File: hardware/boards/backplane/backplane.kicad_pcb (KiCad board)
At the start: 4 copper layers, 151.8 x 30.8 mm, 90 parts, among them J1 XT30U_2+2, J10 SWD, J11 12V 3-WIRE FAN, J12 DS18B20 EXT SUPPLY, J2 XT30U_2+2, J3 XT30U_2+2, J4 XT30U_2+2, J5 XT30U_2+2, J6 XT30U_2+2, J7 XY308-2.54-3P / EXTERNAL CAN, J8 DC IN, J9 12V 3-WIRE FAN, Q1 AO3407A, Q2 2N7002, Q3 AO3407A, Q4 2N7002, U1 STM32C092GCU6, U2 LM5164DDAR, U3 LM5164DDAR, U4 INA237AIDGSR, U5 TCAN3413DR

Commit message: Checkpoint review artifacts and prototype layout refinements
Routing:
- net GND: track 57.7 -> 57.1 mm, vias 66 -> 70
- net VIN_RAW: track 5.21 -> 5.75 mm
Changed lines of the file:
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@@
 	)
 	(segment
-		(start 108.609552 72.588273)
-		(end 108.609552 73.254047)
-		(width 0.2)
-		(layer "F.Cu")
-		(net "GND")
-	)
-	(segment
 		(start 74.603519 50.287638)
 		(end 74.299136 50.592021)
@@
 	)
 	(via
+		(at 109.212052 72.015233)
+		(size 0.6)
+		(drill 0.3)
+		(layers "F.Cu" "B.Cu")
+		(net "GND")
+	)
+	(via
 		(at 109.5425 57.420624)
 		(size 0.6)
@@
 	)
 	(via
-		(at 164.699054 68.604999)
+		(at 131.53 76.517182)
 		(size 0.6)
 		(drill 0.3)
@@
 	)
 	(via
-		(at 131.53 76.517182)
+		(at 137.77 76.517182)
 		(size 0.6)
 		(drill 0.3)
@@
 	)
 	(via
-		(at 137.77 76.517182)
+		(at 113.283564 76.7)
 		(size 0.6)
 		(drill 0.3)
 		(layers "F.Cu" "B.Cu")
-		(free yes)
 		(net "GND")
 	)
@@
 	)
 	(via
+		(at 114.999552 74.787302)
+		(size 0.6)
+		(drill 0.3)
+		(layers "F.Cu" "B.Cu")
+		(net "GND")
+	)
+	(via
 		(at 173.16272 72.052896)
 		(size 0.6)
@@
 	)
 	(via
+		(at 164.137319 67.764828)
+		(size 0.6)
+		(drill 0.3)
+		(layers "F.Cu" "B.Cu")
+		(free yes)
+		(net "GND")
+	)
+	(via
 		(at 75.774011 53.09876)
 		(size 0.6)
@@
 	)
 	(via
+		(at 118.259552 74.787302)
+		(size 0.6)
+		(drill 0.3)
+		(layers "F.Cu" "B.Cu")
+		(net "GND")
+	)
+	(via
 		(at 173.16272 74.352544)
 		(size 0.6)
@@
 	)
 	(via
-		(at 161.836855 68.604999)
+		(at 161.836855 65.295)
 		(size 0.6)
 		(drill 0.3)
@@
 	)
 	(via
-		(at 161.836855 65.295)
+		(at 75.774011 57.420624)
 		(size 0.6)
 		(drill 0.3)
@@
 	)
 	(via
-		(at 75.774011 57.420624)
+		(at 162.411231 67.78024)
 		(size 0.6)
 		(drill 0.3)
@@
 	)
 	(segment
-		(start 165.5975 69.38569)
-		(end 165.5975 67.5625)
+		(start 166.717857 71.254645)
+		(end 167.039487 71.254645)
 		(width 0.2)
 		(layer "F.Cu")
@@
 	)
 	(segment
-		(start 167.039487 70.827677)
-		(end 167.039487 71.304645)
+		(start 165.108243 69.645031)
+		(end 166.717857 71.254645)
 		(width 0.2)
 		(layer "F.Cu")
@@
 	)
 	(segment
-		(start 165.5975 69.38569)
-		(end 167.039487 70.827677)
+		(start 165.108243 68.051757)
+		(end 165.108243 69.645031)
 		(width 0.2)
 		(layer "F.Cu")
@@
 	)
 	(segment
-		(start 165.5975 67.5625)
-		(end 166.21 66.95)
+		(start 166.21 66.95)
+		(end 165.108243 68.051757)
 		(width 0.2)
 		(layer "F.Cu")
@@
 	)
 	(segment
-		(start 160.8975 69.007922)
-		(end 159.271816 70.633606)
+		(start 161.539437 68.204437)
+		(end 161.539437 69.750946)
 		(width 0.2)
 		(layer "F.Cu")
@@
 	)
 	(segment
-		(start 159.728882 71.304645)
-		(end 159.271816 71.304645)
+		(start 162.277468 73.853231)
+		(end 159.728882 71.304645)
 		(width 0.2)
 		(layer "F.Cu")
@@
 	)
 	(segment
-		(start 162.277468 73.853231)
-		(end 159.728882 71.304645)
-		(width 0.2)
-		(layer "F.Cu")
-		(net "VCC")
-	)
-	(segment
-		(start 160.8975 69.007922)
-		(end 160.8975 67.5625)
+		(start 161.539437 69.750946)
+		(end 160.953316 70.337067)
 		(width 0.2)
 		(layer "F.Cu")
@@
 	)
 	(segment
-		(start 160.8975 67.5625)
-		(end 160.285 66.95)
-		(width 0.2)
-		(layer "F.Cu")
-		(net "VCC")
-	)
-	(segment
 		(start 150.3225 74.72)
 		(end 151.565 74.72)
@@
 	)
 	(segment
+		(start 160.285 66.95)
+		(end 161.539437 68.204437)
+		(width 0.2)
+		(layer "F.Cu")
+		(net "VCC")
+	)
+	(segment
 		(start 151.565 74.72)
 		(end 153.33 72.955)
@@
 	)
 	(segment
-		(start 159.271816 70.633606)
-		(end 159.271816 71.304645)
+		(start 160.953316 70.337067)
+		(end 160.189394 70.337067)
 		(width 0.2)
 		(layer "F.Cu")
@@
 		(net "VCC")
 	)
+	(segment
+		(start 160.189394 70.337067)
+		(end 159.271816 71.254645)
+		(width 0.2)
+		(layer "F.Cu")
+		(net "VCC")
+	)
 	(via
 		(at 154.15 68.75)
@@
 		(net "VCC")
 		(layer "F.Cu")
-		(name "VIN_BUS_BACK")
+		(name "VIN_BUS_FRONT")
 		(hatch edge 0.5)
 		(priority 1)
@@
 		(polygon
 			(pts
-				(xy 161.82 63.94) (xy 42.55 63.94) (xy 42.55 71.938594) (xy 89.003284 71.938594) (xy 89.003284 69.45)
-				(xy 158.483546 69.45) (xy 158.483546 70.298636) (xy 161.82 70.298636)
+				(xy 161.100644 63.94) (xy 42.55 63.94) (xy 42.55 71.938594) (xy 89.003284 71.938594) (xy 89.003284 69.45)
+				(xy 158.483546 69.45) (xy 158.483546 69.897828) (xy 161.100644 69.897828)
 			)
 		)
@@
 		(polygon
 			(pts
-				(xy 178.801504 62.512966) (xy 164.55 62.512966) (xy 164.55 70.401526) (xy 167.85331 70.401526) (xy 167.85331 70.4)
-				(xy 178.801504 70.4)
+				(xy 178.801504 62.512966) (xy 165.270064 62.512966) (xy 165.516648 69.367624) (xy 166.665067 69.588822)
+				(xy 166.664665 70.400937) (xy 167.85331 70.401526) (xy 167.85331 70.4) (xy 178.801504 70.4)
 			)
 		)
@@
 		(net "VCC")
 		(layer "B.Cu")
-		(name "VCC_FRONT")
+		(name "VCC_BACK")
 		(hatch edge 0.5)
 		(priority 3)
@@
 		(net "VCC")
 		(layer "In1.Cu")
-		(name "VCC_IN2")
+		(name "VCC_IN1")
 		(hatch edge 0.5)
 		(priority 3)
@@
 		(net "VCC")
 		(layer "In2.Cu")
-		(name "VCC_IN1")
+		(name "VCC_IN2_1")
 		(hatch edge 0.5)
 		(priority 3)

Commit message: Refine prototype Kelvin pours and input grounding; add test TODOs
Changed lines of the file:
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@@
 					(thickness 0.15)
 				)
+				(justify mirror)
 			)
 		)
@@
 			(pinfunction "Pin_1_1")
 			(pintype "passive")
+			(zone_connect 2)
 		)
 		(pad "2" thru_hole circle
@@
 			(pinfunction "Pin_2_2")
 			(pintype "passive")
+			(zone_connect 2)
 		)
 		(embedded_fonts no)
@@
 	(segment
 		(start 162.277468 73.853231)
-		(end 159.728882 71.304645)
+		(end 159.678882 71.254645)
 		(width 0.2)
 		(layer "F.Cu")
@@
 	)
 	(segment
+		(start 159.678882 71.254645)
+		(end 159.271816 71.254645)
+		(width 0.2)
+		(layer "F.Cu")
+		(net "VCC")
+	)
+	(segment
 		(start 160.189394 70.337067)
 		(end 159.271816 71.254645)
@@
 		(polygon
 			(pts
-				(xy 161.100644 63.94) (xy 42.55 63.94) (xy 42.55 71.938594) (xy 89.003284 71.938594) (xy 89.003284 69.45)
-				(xy 158.483546 69.45) (xy 158.483546 69.897828) (xy 161.100644 69.897828)
+				(xy 160.8975 63.94) (xy 42.55 63.94) (xy 42.55 71.94) (xy 89 71.94) (xy 89 69.45) (xy 158.48 69.45)
+				(xy 158.48 69.9) (xy 160.8975 69.9)
 			)
 		)
@@
 		(polygon
 			(pts
-				(xy 178.801504 62.512966) (xy 165.270064 62.512966) (xy 165.516648 69.367624) (xy 166.665067 69.588822)
-				(xy 166.664665 70.400937) (xy 167.85331 70.401526) (xy 167.85331 70.4) (xy 178.801504 70.4)
+				(xy 178.8 62.51) (xy 165.5975 62.51) (xy 165.5975 68.625) (xy 166.95 68.625) (xy 166.95 70.4) (xy 178.8 70.4)
 			)
 		)

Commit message: Add PCBWay logo footprint and stage artwork above both boards
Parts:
- added LOGO_PCBWAY: PCBWay_Logo_25mm, mini-rack-power:PCBWay_Logo_25mm, F.Cu at (105.4, 36.7)
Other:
- board text added: "WayWayWay"

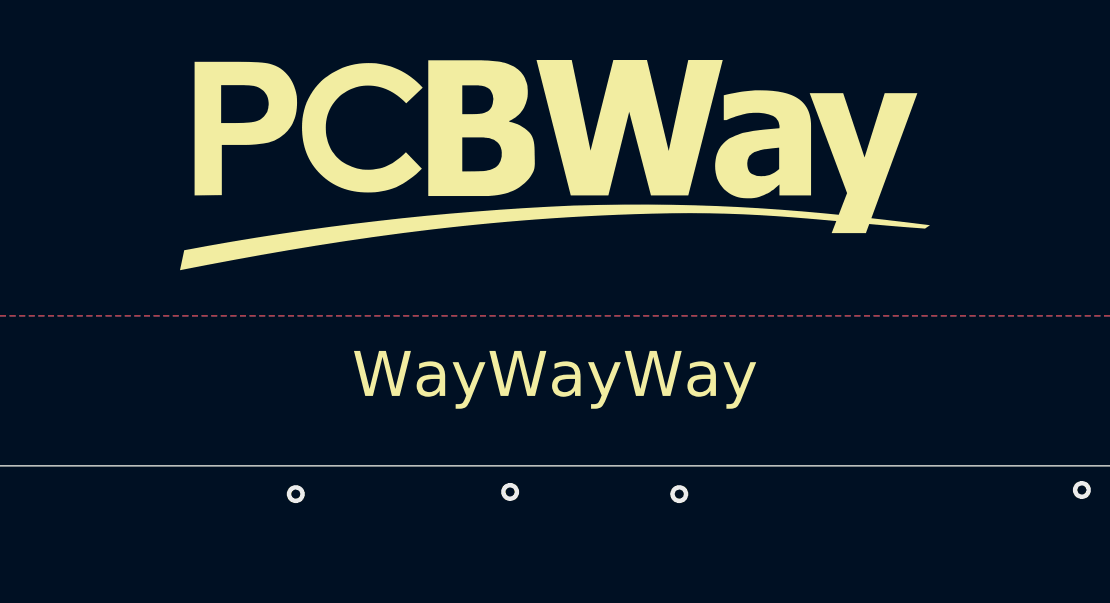
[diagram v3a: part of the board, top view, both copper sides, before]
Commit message: Add 15 mm PCBWay logo and use it on both boards
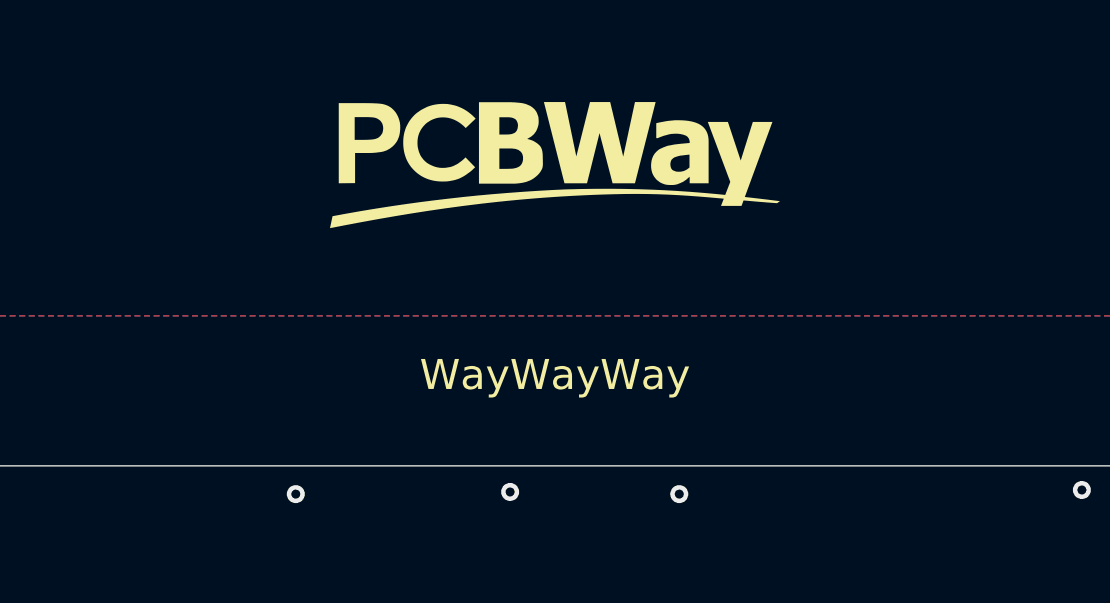
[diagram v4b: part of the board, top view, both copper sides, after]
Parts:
- LOGO_PCBWAY: value PCBWay_Logo_25mm -> PCBWay_Logo_15mm; footprint mini-rack-power:PCBWay_Logo_25mm -> mini-rack-power:PCBWay_Logo_15mm

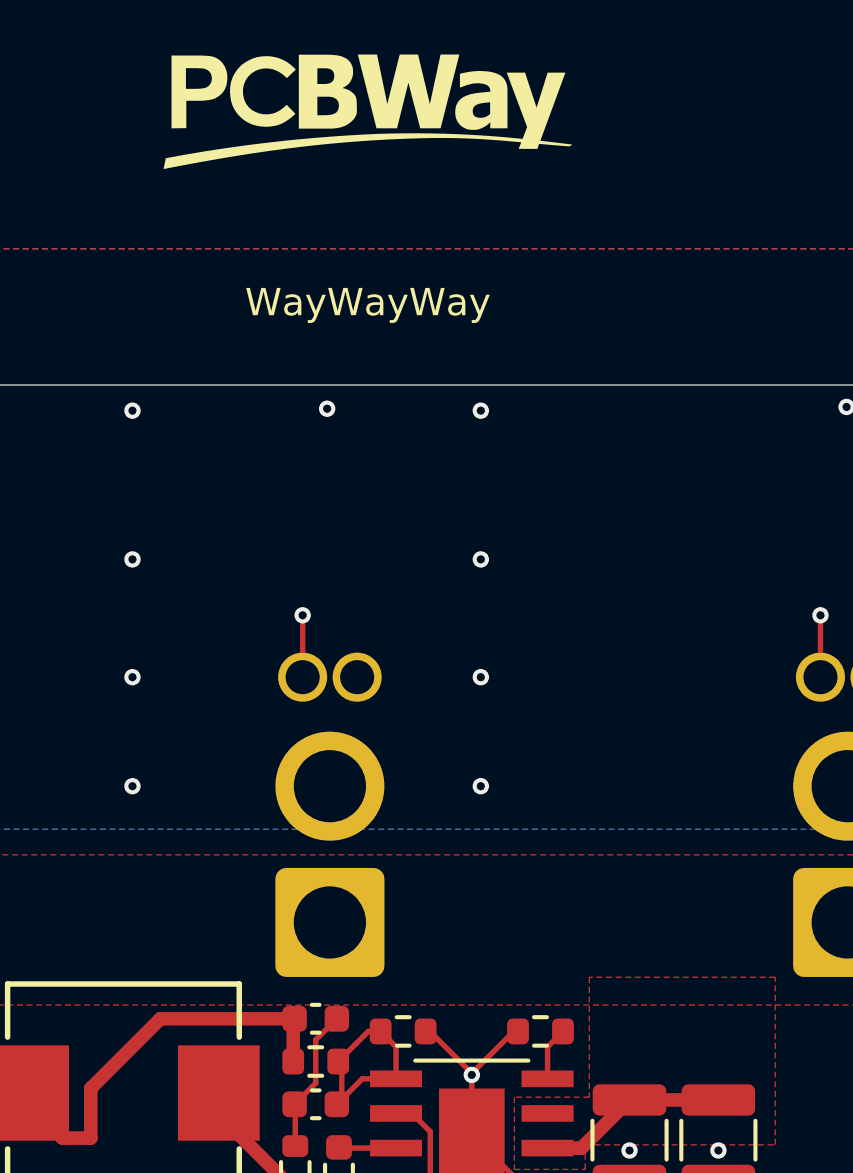
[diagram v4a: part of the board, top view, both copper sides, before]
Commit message: Center backplane PCBWay artwork between slots S02 and S03
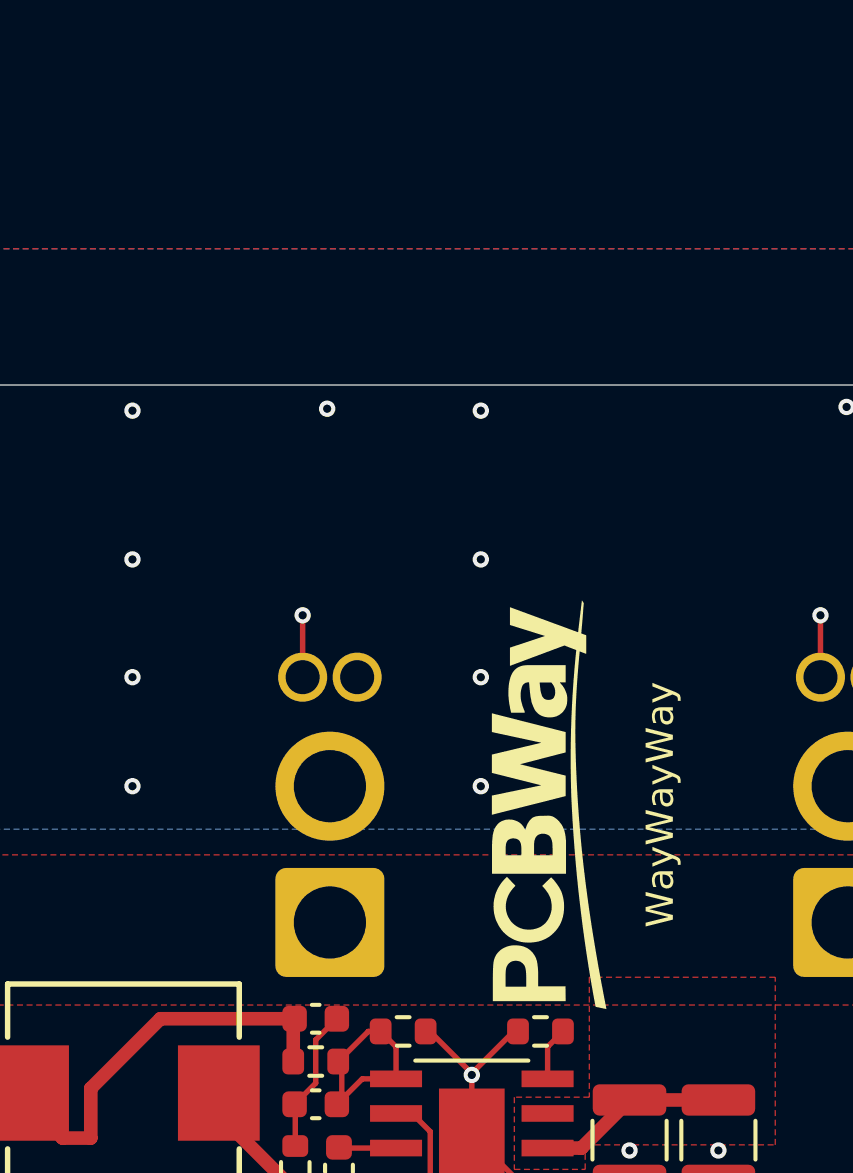
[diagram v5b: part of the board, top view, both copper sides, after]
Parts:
- moved LOGO_PCBWAY 26.3 mm to (112.1, 62.1), turned to 90 degrees
